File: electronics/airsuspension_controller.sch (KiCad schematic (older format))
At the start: 1 part

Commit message: PCB routing done
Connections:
- net +12V_bat: now also conn1.19 (A1), conn1.20 (A2), conn1.21 (A3), conn1.22 (B1); no longer conn1.24 (B3), conn1.25 (C1), conn1.26 (C2), conn1.27 (C3)
- net AirDryer_OUT: now also conn1.31 (E1); no longer conn1.30 (D3)
- net Compressor_OUT: now also conn1.24 (B3), conn1.25 (C1), conn1.26 (C2), conn1.27 (C3); no longer conn1.19 (A1), conn1.20 (A2), conn1.21 (A3), conn1.22 (B1)
- net GNDPWR: now also conn1.30 (D3); no longer conn1.31 (E1)
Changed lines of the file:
@@
 Text Label 9650 5150 2    60   ~ 0
 CAN_RX
-Text Label 2825 2275 0    60   ~ 0
+Text Label 2825 2550 0    60   ~ 0
 Compressor_OUT
-Text GLabel 2825 2400 2    60   Input ~ 0
+Text GLabel 2825 2275 2    60   Input ~ 0
 +12V_bat
 $Comp
 L PWR_FLAG #FLG01
 U 1 1 56FCC0F2
-P 2825 2400
-F 0 "#FLG01" H 2825 2495 50  0001 C CNN
-F 1 "PWR_FLAG" H 2825 2624 50  0001 C CNN
-F 2 "" H 2825 2400 50  0000 C CNN
-F 3 "" H 2825 2400 50  0000 C CNN
-	1    2825 2400
-	-1   0    0    1
+P 2825 2275
+F 0 "#FLG01" H 2825 2370 50  0001 C CNN
+F 1 "PWR_FLAG" H 2825 2499 50  0001 C CNN
+F 2 "" H 2825 2275 50  0000 C CNN
+F 3 "" H 2825 2275 50  0000 C CNN
+	1    2825 2275
+	1    0    0    -1
 $EndComp
 $Comp
 L PWR_FLAG #FLG02
 U 1 1 56FCC0F8
-P 1800 2775
-F 0 "#FLG02" H 1800 2870 50  0001 C CNN
-F 1 "PWR_FLAG" H 1800 2999 50  0001 C CNN
-F 2 "" H 1800 2775 50  0000 C CNN
-F 3 "" H 1800 2775 50  0000 C CNN
-	1    1800 2775
+P 1800 2675
+F 0 "#FLG02" H 1800 2770 50  0001 C CNN
+F 1 "PWR_FLAG" H 1800 2899 50  0001 C CNN
+F 2 "" H 1800 2675 50  0000 C CNN
+F 3 "" H 1800 2675 50  0000 C CNN
+	1    1800 2675
 	1    0    0    -1
 $EndComp
@@
 L GNDPWR #PWR03
 U 1 1 56FCC0FE
-P 1800 2775
-F 0 "#PWR03" H 1800 2575 50  0001 C CNN
-F 1 "GNDPWR" H 1807 2849 50  0001 C CNN
-F 2 "" H 1800 2725 50  0000 C CNN
-F 3 "" H 1800 2725 50  0000 C CNN
-	1    1800 2775
+P 1800 2675
+F 0 "#PWR03" H 1800 2475 50  0001 C CNN
+F 1 "GNDPWR" H 1807 2749 50  0001 C CNN
+F 2 "" H 1800 2625 50  0000 C CNN
+F 3 "" H 1800 2625 50  0000 C CNN
+	1    1800 2675
 	1    0    0    -1
 $EndComp
@@
 Text Label 2825 3150 0    60   ~ 0
 LeftSuck_OUT
-Text Label 2825 2700 0    60   ~ 0
+Text Label 1775 2875 2    60   ~ 0
 AirDryer_OUT
 Text Label 1775 3100 2    60   ~ 0
@@
 	-1   0    0    1
 $EndComp
-Wire Wire Line
-	2200 3225 2200 3275
-Wire Wire Line
-	2200 3275 2825 3275
-Wire Wire Line
-	2450 3225 2450 3150
-Wire Wire Line
-	2450 3150 2825 3150
-Wire Wire Line
-	2200 3375 2825 3375
-Wire Wire Line
-	2200 5075 2200 5250
-Wire Wire Line
-	2200 5250 2825 5250
-Wire Wire Line
-	2450 5075 2450 5125
-Wire Wire Line
-	2450 5125 2825 5125
-Wire Wire Line
-	1950 5075 1950 5125
-Wire Wire Line
-	1950 5125 1775 5125
-Wire Wire Line
-	1950 4925 1950 4900
-Wire Wire Line
-	1950 4900 1775 4900
-Wire Wire Line
-	2200 4775 2200 4825
-Wire Wire Line
-	2200 4825 2825 4825
-Wire Wire Line
-	2450 4775 2450 4725
-Wire Wire Line
-	2450 4725 2825 4725
-Wire Wire Line
-	1950 4775 1775 4775
-Wire Wire Line
-	2200 4625 2200 4675
-Wire Wire Line
-	2200 4675 1775 4675
-Wire Wire Line
-	1950 4625 1950 4575
-Wire Wire Line
-	1950 4575 1775 4575
-Wire Wire Line
-	2450 4625 2825 4625
-Wire Wire Line
-	2200 4475 2200 4525
-Wire Wire Line
-	2200 4525 2825 4525
-Wire Wire Line
-	2450 4475 2450 4425
-Wire Wire Line
-	2450 4425 2825 4425
-Wire Wire Line
-	1950 4475 1775 4475
-Wire Wire Line
-	2200 4325 2200 4375
-Wire Wire Line
-	2200 4375 1775 4375
-Wire Wire Line
-	1950 4325 1950 4275
-Wire Wire Line
-	1950 4275 1775 4275
-Wire Wire Line
-	2450 4325 2825 4325
-Wire Wire Line
-	1800 2775 2200 2775
-Wire Wire Line
-	2200 3075 2200 3000
-Connection ~ 1950 2325
-Wire Wire Line
-	2200 2400 2200 2625
-Wire Wire Line
-	2450 2400 2450 2625
-Wire Wire Line
-	2200 2400 2825 2400
-Connection ~ 2200 2475
-Connection ~ 2450 2400
-Connection ~ 2450 2475
-Wire Wire Line
-	2200 2625 1950 2625
-Wire Wire Line
-	1950 2775 1950 2925
-Connection ~ 1950 2775
-Wire Wire Line
-	2450 2775 2450 2700
-Wire Wire Line
-	2450 2700 2825 2700
-Wire Wire Line
-	2200 2925 2200 2825
-Wire Wire Line
-	2200 2825 2825 2825
-Wire Wire Line
-	2450 2925 2825 2925
-Wire Wire Line
-	2200 3000 1775 3000
-Wire Wire Line
-	2450 3075 2450 3025
-Wire Wire Line
-	2450 3025 2825 3025
-Wire Wire Line
-	1950 3075 1950 3100
-Wire Wire Line
-	1950 3100 1775 3100
-Wire Wire Line
-	1950 3225 1950 3375
-Wire Wire Line
-	1950 3225 1775 3225
-Connection ~ 2450 3375
-Wire Wire Line
-	1950 3525 1950 3475
-Wire Wire Line
-	1950 3475 1775 3475
-Wire Wire Line
-	2200 3525 2200 3600
-Wire Wire Line
-	2200 3600 1775 3600
-Wire Wire Line
-	1950 3675 1950 3725
-Wire Wire Line
-	1950 3725 1775 3725
-Wire Wire Line
-	2200 3675 2200 3850
-Wire Wire Line
-	2200 3850 1775 3850
-Wire Wire Line
-	2450 3675 2450 3850
-Wire Wire Line
-	2450 3850 2825 3850
-Wire Wire Line
-	2450 3525 2450 3600
-Wire Wire Line
-	2450 3600 2825 3600
 $Comp
 L Conn48pin conn1
@@
 	1    0    0    -1
 $EndComp
-Wire Wire Line
-	2200 2275 2200 2325
-Wire Wire Line
-	2450 2275 2450 2325
-Wire Wire Line
-	1950 2275 1950 2475
-Wire Wire Line
-	1950 2275 2825 2275
-Connection ~ 2200 2275
-Connection ~ 2450 2275
-Wire Wire Line
-	2200 4925 2200 5000
-Wire Wire Line
-	2200 5000 1775 5000
-Wire Wire Line
-	2450 4925 2450 4975
-Wire Wire Line
-	2450 4975 2825 4975
 Text Label 4800 2800 2    60   ~ 0
 CompressorTemp_5V
 Text Label 4800 2900 2    60   ~ 0
 CompressorTemp_IN
+Wire Wire Line
+	2200 3225 2200 3275
+Wire Wire Line
+	2200 3275 2825 3275
+Wire Wire Line
+	2450 3225 2450 3150
+Wire Wire Line
+	2450 3150 2825 3150
+Wire Wire Line
+	2200 3375 2825 3375
+Wire Wire Line
+	2200 5075 2200 5250
+Wire Wire Line
+	2200 5250 2825 5250
+Wire Wire Line
+	2450 5075 2450 5125
+Wire Wire Line
+	2450 5125 2825 5125
+Wire Wire Line
+	1950 5075 1950 5125
+Wire Wire Line
+	1950 5125 1775 5125
+Wire Wire Line
+	1950 4925 1950 4900
+Wire Wire Line
+	1950 4900 1775 4900
+Wire Wire Line
+	2200 4775 2200 4825
+Wire Wire Line
+	2200 4825 2825 4825
+Wire Wire Line
+	2450 4775 2450 4725
+Wire Wire Line
+	2450 4725 2825 4725
+Wire Wire Line
+	1950 4775 1775 4775
+Wire Wire Line
+	2200 4625 2200 4675
+Wire Wire Line
+	2200 4675 1775 4675
+Wire Wire Line
+	1950 4625 1950 4575
+Wire Wire Line
+	1950 4575 1775 4575
+Wire Wire Line
+	2450 4625 2825 4625
+Wire Wire Line
+	2200 4475 2200 4525
+Wire Wire Line
+	2200 4525 2825 4525
+Wire Wire Line
+	2450 4475 2450 4425
+Wire Wire Line
+	2450 4425 2825 4425
+Wire Wire Line
+	1950 4475 1775 4475
+Wire Wire Line
+	2200 4325 2200 4375
+Wire Wire Line
+	2200 4375 1775 4375
+Wire Wire Line
+	1950 4325 1950 4275
+Wire Wire Line
+	1950 4275 1775 4275
+Wire Wire Line
+	2450 4325 2825 4325
+Wire Wire Line
+	2200 3075 2200 3000
+Connection ~ 1950 2325
+Wire Wire Line
+	2450 2625 1950 2625
+Connection ~ 1950 2775
+Wire Wire Line
+	2200 2925 2200 2825
+Wire Wire Line
+	2200 2825 2825 2825
+Wire Wire Line
+	2450 2925 2825 2925
+Wire Wire Line
+	2200 3000 1775 3000
+Wire Wire Line
+	2450 3075 2450 3025
+Wire Wire Line
+	2450 3025 2825 3025
+Wire Wire Line
+	1950 3075 1950 3100
+Wire Wire Line
+	1950 3100 1775 3100
+Wire Wire Line
+	1950 3225 1950 3375
+Wire Wire Line
+	1950 3225 1775 3225
+Connection ~ 2450 3375
+Wire Wire Line
+	1950 3525 1950 3475
+Wire Wire Line
+	1950 3475 1775 3475
+Wire Wire Line
+	2200 3525 2200 3600
+Wire Wire Line
+	2200 3600 1775 3600
+Wire Wire Line
+	1950 3675 1950 3725
+Wire Wire Line
+	1950 3725 1775 3725
+Wire Wire Line
+	2200 3675 2200 3850
+Wire Wire Line
+	2200 3850 1775 3850
+Wire Wire Line
+	2450 3675 2450 3850
+Wire Wire Line
+	2450 3850 2825 3850
+Wire Wire Line
+	2450 3525 2450 3600
+Wire Wire Line
+	2450 3600 2825 3600
+Wire Wire Line
+	2200 2275 2200 2475
+Wire Wire Line
+	2450 2275 2450 2325
+Wire Wire Line
+	1950 2275 1950 2475
+Wire Wire Line
+	1950 2275 2825 2275
+Connection ~ 2200 2275
+Connection ~ 2450 2275
+Wire Wire Line
+	2200 4925 2200 5000
+Wire Wire Line
+	2200 5000 1775 5000
+Wire Wire Line
+	2450 4925 2450 4975
+Wire Wire Line
+	2450 4975 2825 4975
+Connection ~ 2200 2625
+Wire Wire Line
+	2450 2475 2450 2625
+Wire Wire Line
+	2825 2550 2450 2550
+Connection ~ 2450 2550
+Connection ~ 2200 2325
+Connection ~ 2200 2775
+Wire Wire Line
+	1950 2925 1925 2925
+Wire Wire Line
+	1950 2775 1950 2675
+Wire Wire Line
+	1950 2675 1800 2675
+Wire Wire Line
+	1950 2775 2450 2775
+Wire Wire Line
+	1925 2925 1925 2875
+Wire Wire Line
+	1925 2875 1775 2875
 $EndSCHEMATC

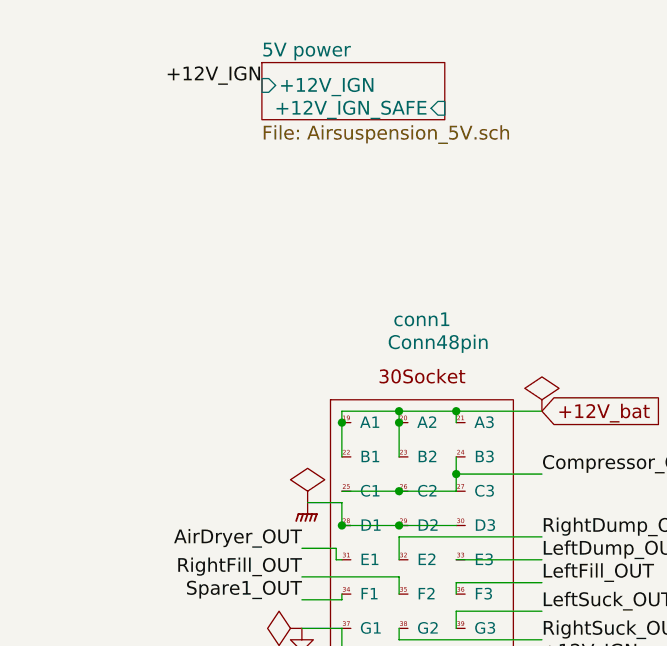
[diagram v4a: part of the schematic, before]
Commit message: Some updates as some parts were not available
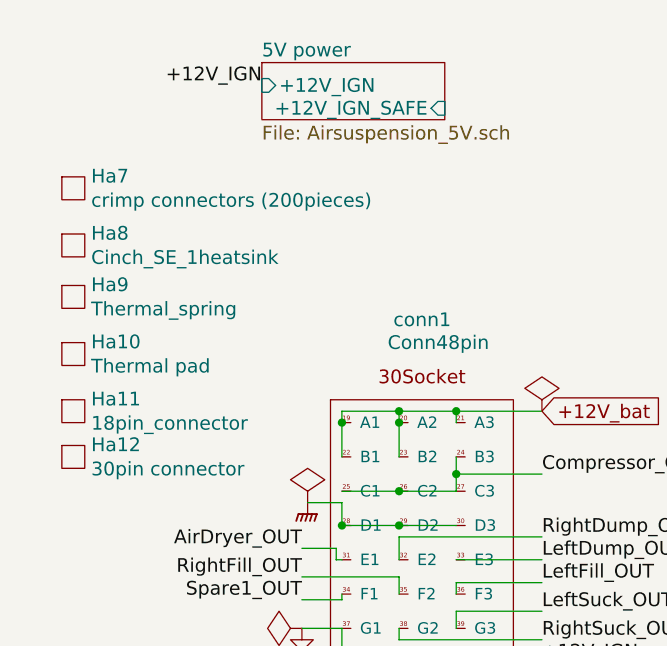
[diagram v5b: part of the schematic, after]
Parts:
- added Ha10: Thermal pad, symbol Hardware
- added Ha11: 18pin_connector, symbol Hardware
- added Ha12: 30pin connector, symbol Hardware
- added Ha7: crimp connectors (200pieces), symbol Hardware
- added Ha8: Cinch_SE_1heatsink, symbol Hardware
- added Ha9: Thermal_spring, symbol Hardware
- conn1: farnell 1282187 -> 1282184; part 5810148005 -> 5810148007
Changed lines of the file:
@@
 F 2 "cinch:Conn48pin" H 2450 2525 60  0001 C CNN
 F 3 "http://www.farnell.com/datasheets/49878.pdf" H 2450 2525 60  0001 C CNN
-F 4 "1282187" H 2300 3525 60  0001 C CNN "farnell"
-F 5 "5810148005" H 2300 3525 60  0001 C CNN "part"
+F 4 "1282184" H 2300 3525 60  0001 C CNN "farnell"
+F 5 "5810148007" H 2300 3525 60  0001 C CNN "part"
 	1    2300 3525
 	1    0    0    -1
@@
 Wire Wire Line
 	1925 2875 1775 2875
+$Comp
+L Hardware Ha8
+U 1 1 56FF0A6B
+P 775 1550
+F 0 "Ha8" H 853 1603 60  0000 L CNN
+F 1 "Cinch_SE_1heatsink" H 853 1497 60  0000 L CNN
+F 2 "" H 775 1575 60  0000 C CNN
+F 3 "" H 775 1575 60  0000 C CNN
+F 4 "5810130042" H 775 1550 60  0001 C CNN "part"
+F 5 "1282197" H 775 1550 60  0001 C CNN "farnell"
+	1    775  1550
+	1    0    0    -1
+$EndComp
+$Comp
+L Hardware Ha9
+U 1 1 56FF0F10
+P 775 1775
+F 0 "Ha9" H 853 1828 60  0000 L CNN
+F 1 "Thermal_spring" H 853 1722 60  0000 L CNN
+F 2 "" H 775 1800 60  0000 C CNN
+F 3 "" H 775 1800 60  0000 C CNN
+F 4 "5810000021" H 775 1775 60  0001 C CNN "part"
+F 5 "1282203" H 775 1775 60  0001 C CNN "farnell"
+	1    775  1775
+	1    0    0    -1
+$EndComp
+$Comp
+L Hardware Ha10
+U 1 1 56FF13B6
+P 775 2025
+F 0 "Ha10" H 853 2078 60  0000 L CNN
+F 1 "Thermal pad" H 853 1972 60  0000 L CNN
+F 2 "" H 775 2050 60  0000 C CNN
+F 3 "" H 775 2050 60  0000 C CNN
+F 4 "FCTS73-05N" H 775 2025 60  0001 C CNN "part"
+F 5 "2289473" H 775 2025 60  0001 C CNN "farnell"
+	1    775  2025
+	1    0    0    -1
+$EndComp
+$Comp
+L Hardware Ha7
+U 1 1 56FF381D
+P 775 1300
+F 0 "Ha7" H 853 1353 60  0000 L CNN
+F 1 "crimp connectors (200pieces)" H 853 1247 60  0000 L CNN
+F 2 "" H 775 1325 60  0000 C CNN
+F 3 "" H 775 1325 60  0000 C CNN
+F 4 "4250000873" H 775 1300 60  0001 C CNN "part"
+F 5 "1282210" H 775 1300 60  0001 C CNN "farnell"
+	1    775  1300
+	1    0    0    -1
+$EndComp
+$Comp
+L Hardware Ha11
+U 1 1 56FF3F46
+P 775 2275
+F 0 "Ha11" H 853 2328 60  0000 L CNN
+F 1 "18pin_connector" H 853 2222 60  0000 L CNN
+F 2 "" H 775 2300 60  0000 C CNN
+F 3 "" H 775 2300 60  0000 C CNN
+F 4 "5810118023" H 775 2275 60  0001 C CNN "part"
+F 5 "1282205" H 775 2275 60  0001 C CNN "farnell"
+	1    775  2275
+	1    0    0    -1
+$EndComp
+$Comp
+L Hardware Ha12
+U 1 1 56FF4D0E
+P 775 2475
+F 0 "Ha12" H 853 2528 60  0000 L CNN
+F 1 "30pin connector" H 853 2422 60  0000 L CNN
+F 2 "" H 775 2500 60  0000 C CNN
+F 3 "" H 775 2500 60  0000 C CNN
+F 4 "5810130028" H 775 2475 60  0001 C CNN "part"
+F 5 "1282206" H 775 2475 60  0001 C CNN "farnell"
+	1    775  2475
+	1    0    0    -1
+$EndComp
 $EndSCHEMATC
